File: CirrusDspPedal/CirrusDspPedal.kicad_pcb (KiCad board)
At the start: 2 copper layers, 112.5 x 86.4 mm, 92 parts, among them J1 MonoJack2Switch, J2 MonoJack2Switch, J3 Conn_02x05_Odd_Even, J4 Barrel_Jack_Switch, J5 MonoJack2Switch, J6 Micro_SD_Card, J7 Conn_01x01, K1 HFD4/3_S, Q1 DMG2302U, SW1 P26L-1D-RND MTL, SW2 P26L-1D-RND MTL, SW3 SW_SPST, SW4 SW_SPST, U1 CS5343, U2 74AHC1G126, U3 CS4344, U4 SE8250X2_SOT23, U5 MCP1703A-1202_SOT223, U6 MCP601-xOT, U7 STM32F405RGTx

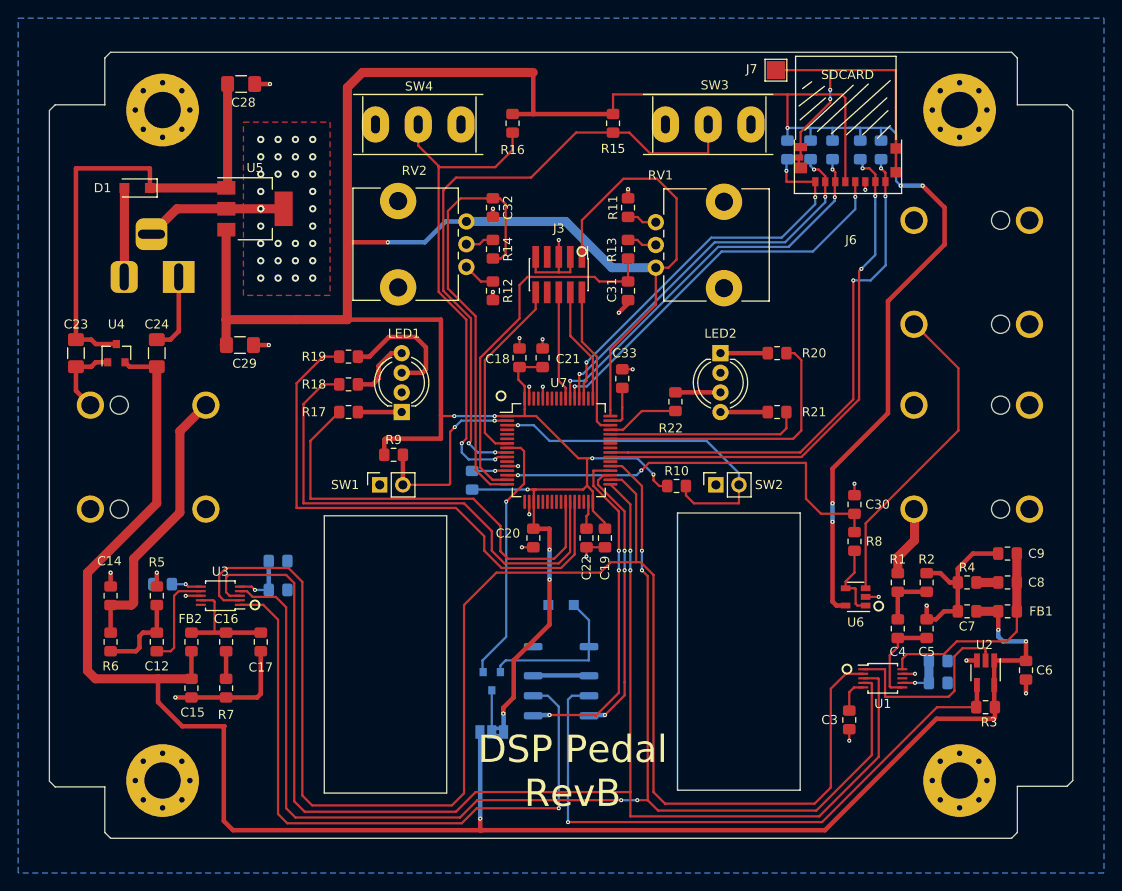
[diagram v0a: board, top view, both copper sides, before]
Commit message: Updated RevB
- Replaced analog pots with Rotary Encoders
- Added I2C connector (for OLED screen)
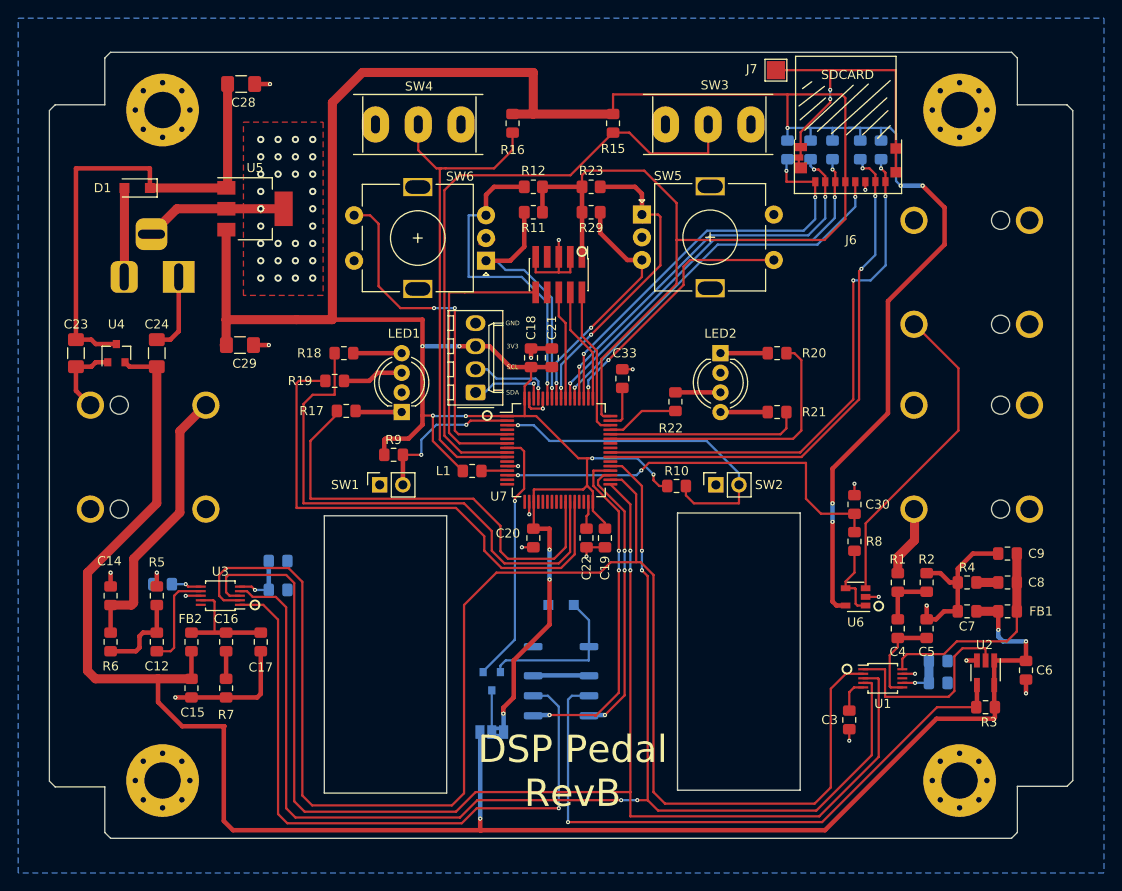
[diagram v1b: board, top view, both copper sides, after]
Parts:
- removed C31, C32: 100nF, Capacitor_SMD:C_0805_2012Metric_Pad1.15x1.40mm_HandSolder
- removed R13, R14: 50R, Resistor_SMD:R_0805_2012Metric_Pad1.15x1.40mm_HandSolder
- removed RV1, RV2: RK09L1140A65, Potentiometer_THT:Potentiometer_Alps_RK09L_Single_Vertical
- added J8: Conn_01x04, Connector_Molex:Molex_KK-254_AE-6410-04A_1x04_P2.54mm_Vertical, F.Cu at (139.2, 91.9)
- added R23: 10K, Resistor_SMD:R_0805_2012Metric_Pad1.20x1.40mm_HandSolder, F.Cu at (151.9, 69.3)
- added R29: 10K, Resistor_SMD:R_0805_2012Metric_Pad1.20x1.40mm_HandSolder, F.Cu at (151.9, 72.1)
- added SW5: Rotary_Encoder_Switch, Rotary_Encoder:RotaryEncoder_Alps_EC11E-Switch_Vertical_H20mm, F.Cu at (157.5, 72.4)
- added SW6: Rotary_Encoder_Switch, Rotary_Encoder:RotaryEncoder_Alps_EC11E-Switch_Vertical_H20mm, F.Cu at (140.3, 77.5)
- L1: moved to F.Cu
- R11, R12: value 100R -> 10K; footprint Resistor_SMD:R_0805_2012Metric_Pad1.15x1.40mm_HandSolder -> Resistor_SMD:R_0805_2012Metric_Pad1.20x1.40mm_HandSolder
- moved R12 12.3 mm to (145.5, 69.3), turned to 180 degrees
- moved R11 10.4 mm to (145.5, 72.1), turned to 180 degrees
- moved R18 3.47 mm to (124.7, 87.6)
- moved R19 3.07 mm to (123.7, 90.7)
- moved C18 1.27 mm to (145.3, 88.1)
- moved C21 1.02 mm to (147.6, 88.1)
- moved L1 1.02 mm to (138.8, 100.6), turned to 0 degrees
- moved R17 0.28 mm to (125.0, 94.0)
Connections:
- R11 pad 1: Net-(R11-Pad1) -> +3V3
- R11 pad 2: GND -> /ExtInput/Encoder2_ENC_A
- R12 pad 1: Net-(R12-Pad1) -> +3V3
- R12 pad 2: GND -> /ExtInput/Encoder2_ENC_B
- U7 pad 15: /ExtInput/UserPotA_IN -> Net-(U7-Pad15)
- U7 pad 16: /ExtInput/UserPotB_IN -> Net-(U7-Pad16)
- U7 pad 5: Net-(U7-Pad5) -> /ExtInput/Encoder2_ENC_SW
- U7 pad 50: Net-(U7-Pad50) -> /ExtInput/Encoder1_ENC_SW
- U7 pad 56: Net-(U7-Pad56) -> /ExtInput/Encoder1_ENC_A
- U7 pad 57: Net-(U7-Pad57) -> /ExtInput/Encoder1_ENC_B
- U7 pad 58: Net-(U7-Pad58) -> /ExtInput/Encoder2_ENC_A
- U7 pad 59: Net-(U7-Pad59) -> /ExtInput/Encoder2_ENC_B
- U7 pad 61: Net-(U7-Pad61) -> /SignalProcessing/OLED_SCL
- U7 pad 62: Net-(U7-Pad62) -> /SignalProcessing/OLED_SDA
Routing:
- net /ExtInput/UserPotB_IN: track 48.8 -> 0.00 mm
- net /ExtInput/UserPotA_IN: track 40.4 -> 0.00 mm
- net /ExtInput/Encoder2_ENC_SW: track 0.00 -> 38.7 mm, vias 0 -> 2
- net /ExtInput/Encoder2_ENC_B: track 0.00 -> 35.9 mm, vias 0 -> 1
- net /ExtInput/Encoder1_ENC_A: track 0.00 -> 34.7 mm, vias 0 -> 2
- net /ExtInput/Encoder1_ENC_SW: track 0.00 -> 29.1 mm, vias 0 -> 2
- net /ExtInput/Encoder2_ENC_A: track 0.00 -> 28.7 mm, vias 0 -> 1
- net /ExtInput/Encoder1_ENC_B: track 0.00 -> 27.2 mm, vias 0 -> 2
- net /SignalProcessing/NRST: track 20.7 -> 31.8 mm
- net /SignalProcessing/OLED_SCL: track 0.00 -> 9.34 mm, vias 0 -> 1
- net /SignalProcessing/OLED_SDA: track 0.00 -> 8.44 mm, vias 0 -> 1
- net Net-(LED1-Pad3): track 14.1 -> 6.71 mm
- net +3V3: track 419.2 -> 426.0 mm
- net /ExtInput/FootSwitchA_IN: track 21.0 -> 17.3 mm
- net /SignalProcessing/LEDA_G: track 55.1 -> 58.8 mm
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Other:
- board text added: "GND"
- board text added: "SCL"
- board text added: "SDA"

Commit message: updated revB
- Added higher out current LDO (LD1117) for 5V rail
- Added jumper on OLED connector to select 3V3/5V
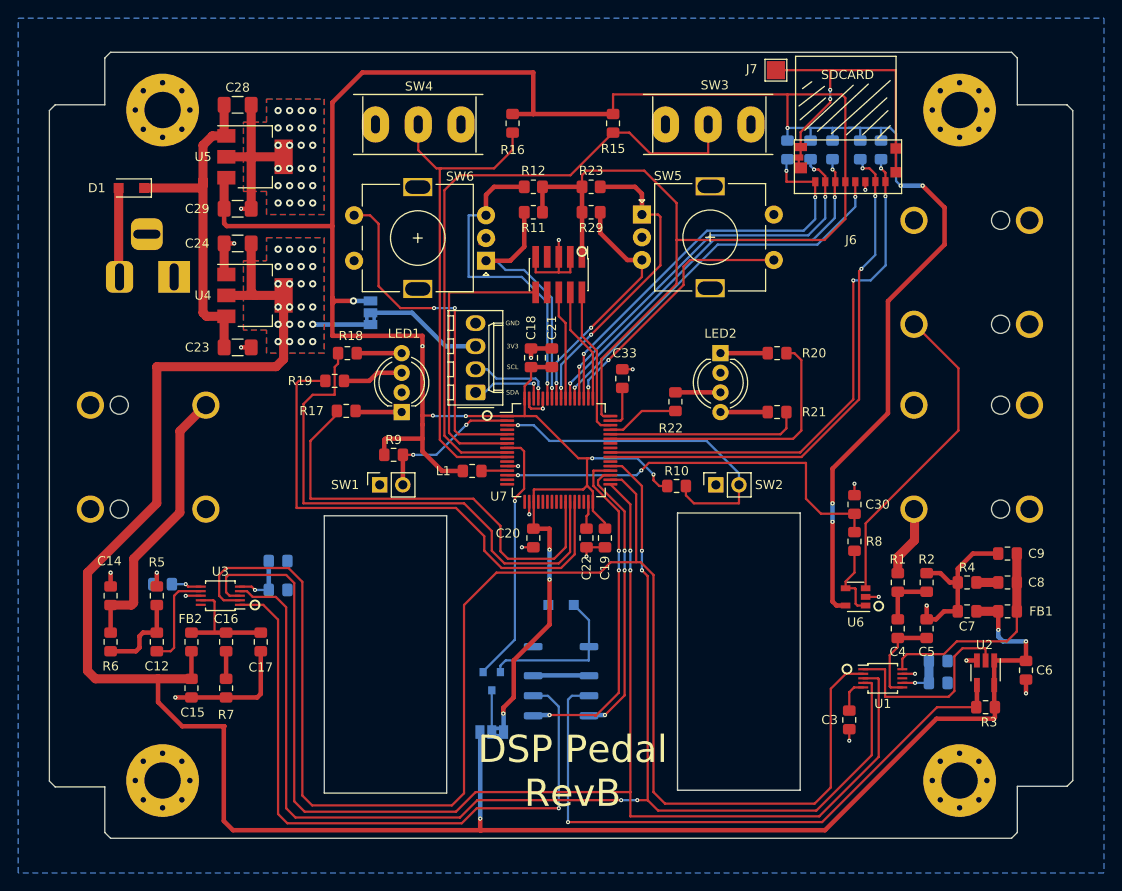
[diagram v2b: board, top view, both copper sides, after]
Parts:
- added JP1: Jumper_3_Bridged12, Jumper:SolderJumper-3_P1.3mm_Bridged2Bar12_Pad1.0x1.5mm, B.Cu at (127.6, 83.2)
- C23: value 1uF -> 100nF 25V
- C24: value 1uF -> 10uF
- C28: value 1uF -> 1uF 25V
- U4: value SE8250X2_SOT23 -> LD1117S50TR_SOT223; footprint Package_TO_SOT_SMD:SOT-23 -> Package_TO_SOT_SMD:SOT-223-3_TabPin2
- moved C23 17.8 mm to (113.0, 87.0), turned to 0 degrees
- moved U4 16.5 mm to (114.9, 81.3), turned to 0 degrees
- moved C29 15.0 mm to (113.0, 71.8)
- moved C24 15.0 mm to (113.0, 75.6), turned to 180 degrees
- moved U5 5.71 mm to (114.9, 66.0)
- moved C28 2.32 mm to (113.0, 60.3)
- moved D1 0.63 mm to (101.3, 69.5)
- moved J4 0.51 mm to (106.0, 79.2)
- moved R18 0.38 mm to (125.1, 87.6)
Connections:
- J8 pad 3: +3V3 -> Net-(J8-Pad3)
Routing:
- net +5V: track 197.7 -> 233.9 mm, vias 3 -> 27
- net +3V3: track 426.0 -> 406.8 mm
- net Net-(C23-Pad1): track 53.7 -> 38.4 mm
- net Net-(J8-Pad3): track 0.00 -> 13.1 mm
- net GND: track 112.0 -> 100.1 mm, vias 52 -> 47
- net /ExtInput/FootSwitchA_IN: track 17.3 -> 16.3 mm
- added copper zone on B.Cu, net +5V
- added copper zone on F.Cu, net +5V
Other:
- rule pad_to_mask_clearance: 0.05 -> 0
- board text added: "<- OLED"

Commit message: updated revb
- Added input amp with charge pump and protection diodes
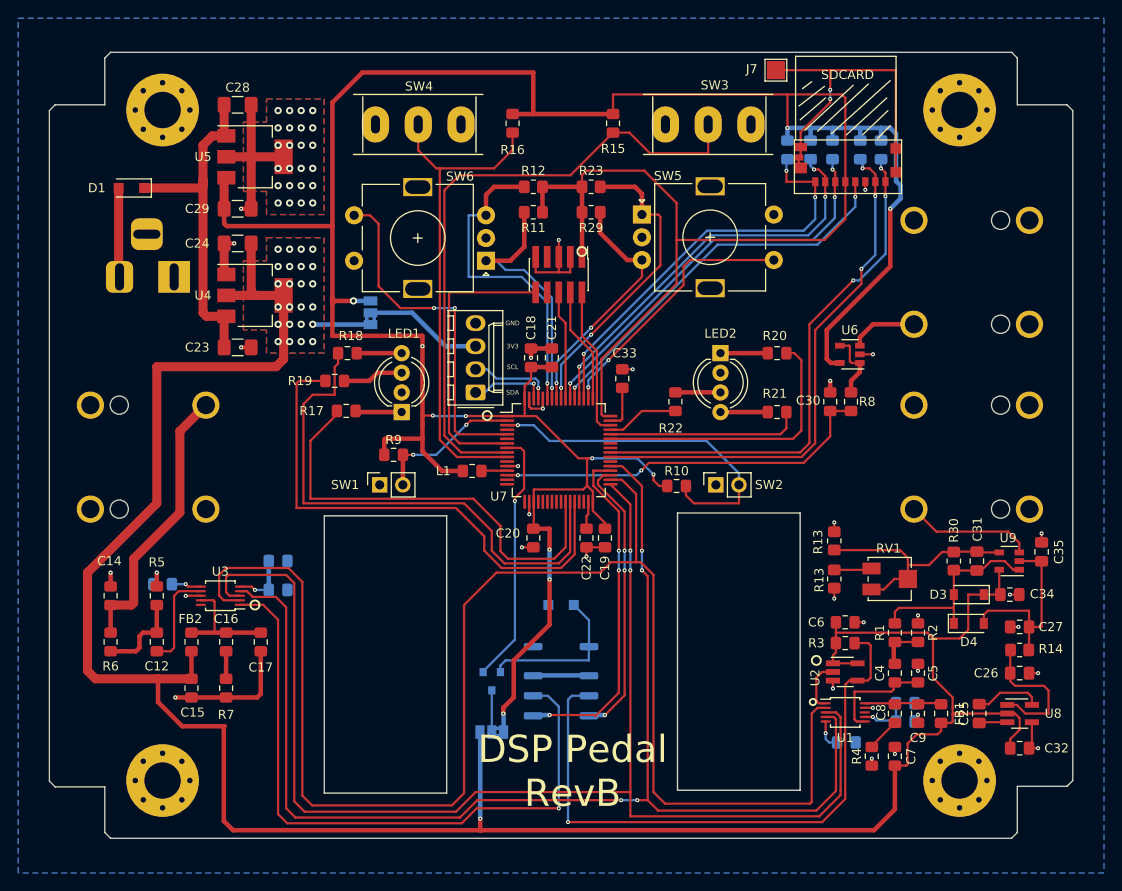
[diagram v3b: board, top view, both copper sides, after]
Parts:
- added C25: 1uF, Capacitor_SMD:C_0805_2012Metric_Pad1.18x1.45mm_HandSolder, F.Cu at (194.6, 127.3)
- added C26: 1uF, Capacitor_SMD:C_0805_2012Metric_Pad1.18x1.45mm_HandSolder, F.Cu at (199.0, 122.8)
- added C27: 100nF, Capacitor_SMD:C_0805_2012Metric_Pad1.18x1.45mm_HandSolder, F.Cu at (199.0, 117.7)
- added C31: 270pF, Capacitor_SMD:C_0805_2012Metric_Pad1.18x1.45mm_HandSolder, F.Cu at (194.3, 110.5)
- added C32: 1uF, Capacitor_SMD:C_0805_2012Metric_Pad1.18x1.45mm_HandSolder, F.Cu at (199.0, 131.1)
- added C34: 100nF, Capacitor_SMD:C_0805_2012Metric_Pad1.18x1.45mm_HandSolder, F.Cu at (197.9, 114.2)
- added C35: 100nF, Capacitor_SMD:C_0805_2012Metric_Pad1.18x1.45mm_HandSolder, F.Cu at (201.4, 109.5)
- added D3: 1N5817, Diode_SMD:D_SOD-123, F.Cu at (193.4, 114.2)
- added D4: 1N5817, Diode_SMD:D_SOD-123, F.Cu at (193.4, 117.3)
- added R13: 4K7, Resistor_SMD:R_0805_2012Metric_Pad1.20x1.40mm_HandSolder, F.Cu at (178.6, 112.5)
- added R13: 10K, Resistor_SMD:R_0805_2012Metric_Pad1.20x1.40mm_HandSolder, F.Cu at (178.6, 108.3)
- added R14: 47R, Resistor_SMD:R_0805_2012Metric_Pad1.20x1.40mm_HandSolder, F.Cu at (199.0, 120.3)
- added R30: 100K, Resistor_SMD:R_0805_2012Metric_Pad1.20x1.40mm_HandSolder, F.Cu at (191.8, 110.5)
- added RV1: 500K, Potentiometer_SMD:Potentiometer_Bourns_3314J_Vertical, F.Cu at (184.7, 112.5)
- added U8: TPS60400, Package_TO_SOT_SMD:SOT-23-5_HandSoldering, F.Cu at (199.0, 127.3)
- added U9: OPA209AIDBV, Package_TO_SOT_SMD:SOT-23-5, F.Cu at (197.9, 110.5)
- C3: moved to B.Cu
- moved U6 26.7 mm to (180.3, 87.8)
- moved R4 21.8 mm to (182.8, 132.0), turned to 270 degrees
- moved C6 20.6 mm to (179.8, 117.2), turned to 0 degrees
- moved C9 20.2 mm to (187.8, 127.3), turned to 270 degrees
- moved C8 19.0 mm to (185.3, 127.3), turned to 270 degrees
- moved C7 17.8 mm to (185.3, 132.0), turned to 90 degrees
- moved R3 17.0 mm to (179.8, 119.5), turned to 180 degrees
- moved U2 15.4 mm to (179.8, 122.7), turned to 0 degrees
- moved R8 15.4 mm to (180.5, 93.0), turned to 90 degrees
- moved FB1 13.4 mm to (190.4, 127.3), turned to 270 degrees
- moved C30 11.6 mm to (178.2, 93.0)
- moved C1 5.88 mm to (186.4, 126.1)
- moved R2 5.61 mm to (187.8, 118.4)
- moved C2 5.59 mm to (186.4, 128.1)
- moved U1 5.57 mm to (179.8, 127.1)
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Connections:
- R1 pad 2: Net-(J1-Pad1) -> Net-(C31-Pad1)
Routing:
- net +5V: track 233.9 -> 267.5 mm, vias 27 -> 25
- net +3V3: track 406.8 -> 375.0 mm, vias 14 -> 11
- net Net-(J5-Pad1): track 35.3 -> 7.52 mm
- net Net-(C31-Pad2): track 0.00 -> 26.1 mm
- net Net-(C31-Pad1): track 0.00 -> 22.2 mm
- net -5V: track 0.00 -> 21.0 mm
- net /InputSignal/SDOUT: track 22.3 -> 5.76 mm
- net Net-(C26-Pad1): track 0.00 -> 15.5 mm
- net /InputSignal/VA: track 23.5 -> 8.85 mm
- net Net-(C25-Pad2): track 0.00 -> 7.38 mm
- net GND: track 100.1 -> 93.0 mm, vias 47 -> 57
- net /InputSignal/ADIN_SCLK: track 171.9 -> 165.4 mm
- net Net-(J1-Pad1): track 7.83 -> 14.3 mm
- net /InputSignal/ADIN_LRCK: track 151.4 -> 145.7 mm
- net /InputSignal/ADIN_MCLK: track 144.5 -> 139.4 mm
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
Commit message: updated revb
- Moved THT components to improve UX layout
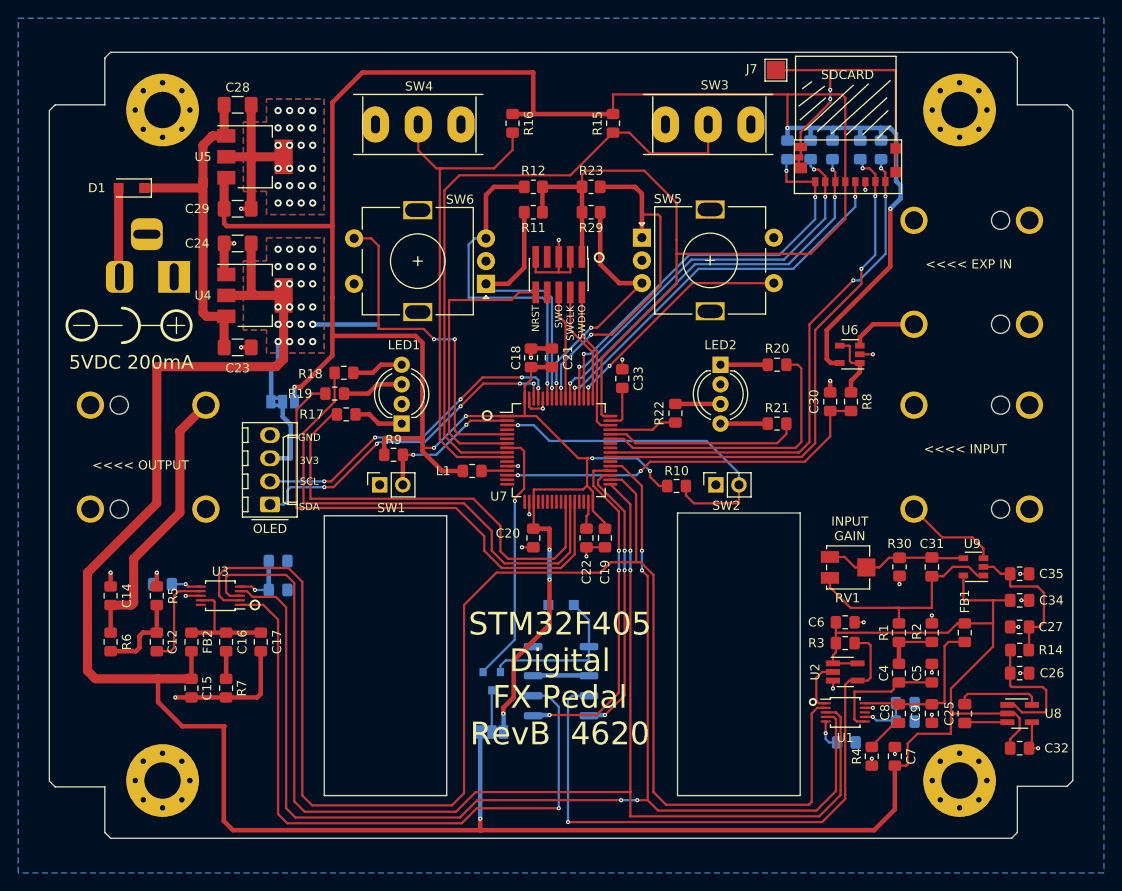
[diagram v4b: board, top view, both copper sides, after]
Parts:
- removed D3, D4: 1N5817, Diode_SMD:D_SOD-123
- removed R13: 4K7, Resistor_SMD:R_0805_2012Metric_Pad1.20x1.40mm_HandSolder
- removed R13: 10K, Resistor_SMD:R_0805_2012Metric_Pad1.20x1.40mm_HandSolder
- RV1: value 500K -> 100K
- moved J8 25.7 mm to (116.6, 104.3)
- moved JP1 13.7 mm to (118.0, 93.0), turned to 0 degrees
- moved FB1 9.26 mm to (193.0, 118.4), turned to 90 degrees
- moved R30 6.00 mm to (185.8, 111.1), turned to 270 degrees
- moved C31 4.99 mm to (189.4, 111.1)
- moved RV1 4.75 mm to (180.1, 111.2)
- moved U9 3.99 mm to (193.9, 111.1)
- moved C35 3.41 mm to (199.0, 111.9), turned to 0 degrees
- moved SW5 2.54 mm to (157.5, 74.9)
- moved SW6 2.54 mm to (140.3, 80.0)
- moved R18 2.19 mm to (124.7, 89.8)
- moved C25 1.59 mm to (193.0, 127.3)
- moved C5 1.52 mm to (189.4, 122.8)
- moved C9 1.52 mm to (189.4, 127.3)
- moved R2 1.52 mm to (189.4, 118.4)
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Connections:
- R30 pad 1: Net-(C31-Pad1) -> Net-(C31-Pad2)
- R30 pad 2: Net-(C31-Pad2) -> GND
- RV1 pad 1: Net-(R13-Pad1) -> Net-(C31-Pad2)
- RV1 pad 3: Net-(C31-Pad2) -> Net-(C31-Pad1)
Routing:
- net /SignalProcessing/OLED_SDA: track 8.44 -> 36.8 mm, vias 1 -> 5
- net /SignalProcessing/OLED_SCL: track 9.34 -> 36.4 mm, vias 1 -> 5
- net +5V: track 267.5 -> 281.1 mm
- net Net-(C31-Pad2): track 26.1 -> 16.2 mm
- net /InputSignal/VA: track 8.85 -> 17.9 mm
- net +3V3: track 375.0 -> 381.0 mm, vias 11 -> 10
- net -5V: track 21.0 -> 16.3 mm
- net Net-(J8-Pad3): track 13.1 -> 8.88 mm
- net Net-(R13-Pad1): track 4.16 -> 0.00 mm
- net /SignalProcessing/LEDA_G: track 59.0 -> 55.1 mm
- net /ExtInput/Encoder1_ENC_A: track 34.7 -> 38.5 mm
- net GND: track 93.0 -> 89.2 mm, vias 57 -> 56
- net Net-(J1-Pad1): track 14.3 -> 10.6 mm
- net Net-(C31-Pad1): track 22.2 -> 25.4 mm
- net /ExtInput/Encoder1_ENC_SW: track 29.1 -> 26.4 mm
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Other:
- outline, holes or cut-outs redrawn
- board text added: "5VDC 200mA"
- board text added: "<<<< EXP IN"
- board text added: "<<<< INPUT"
- board text added: "<<<< OUTPUT"
- board text added: "INPUT GAIN"
- board text added: "NRST"
- board text added: "OLED"
- board text added: "STM32F405 Digital FX Pedal RevB 4620"
- board text added: "SWCLK"
- board text added: "SWDIO"
- board text added: "SWO"
- board text removed: "DSP Pedal RevB"

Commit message: final revb layout
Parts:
- added D3: LED, LED_SMD:LED_0805_2012Metric_Pad1.15x1.40mm_HandSolder, F.Cu at (198.9, 119.3)
- added D4: LED, LED_SMD:LED_0805_2012Metric_Pad1.15x1.40mm_HandSolder, F.Cu at (120.3, 57.4)
- added D5: LED, LED_SMD:LED_0805_2012Metric_Pad1.15x1.40mm_HandSolder, F.Cu at (120.3, 91.7)
- added R13: 2K2, Resistor_SMD:R_0805_2012Metric_Pad1.20x1.40mm_HandSolder, F.Cu at (198.9, 121.9)
- added R31: 2K2, Resistor_SMD:R_0805_2012Metric_Pad1.20x1.40mm_HandSolder, F.Cu at (115.8, 57.4)
- added R32: 2K2, Resistor_SMD:R_0805_2012Metric_Pad1.20x1.40mm_HandSolder, F.Cu at (115.8, 91.7)
- SW5, SW6: value Rotary_Encoder_Switch -> PEC11R-4020K-S0024
- U9: value OPA209AIDBV -> OPA197IDBV
- moved C26 4.59 mm to (195.6, 125.9), turned to 270 degrees
- moved R14 3.56 mm to (198.9, 116.7)
- moved C27 3.56 mm to (198.9, 114.2)
- moved C34 3.18 mm to (198.9, 111.6)
- moved C35 2.79 mm to (198.9, 109.1)
- moved R19 2.16 mm to (125.9, 92.1)
- moved C32 1.73 mm to (199.7, 129.5)
- moved U8 1.62 mm to (199.7, 125.8)
- moved C25 1.46 mm to (193.0, 125.8)
- moved R18 1.14 mm to (125.9, 89.8)
- moved R17 0.89 mm to (125.9, 94.4)
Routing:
- net +5V: track 281.1 -> 290.1 mm
- net Net-(C26-Pad1): track 15.1 -> 21.3 mm
- net +3V3: track 381.0 -> 384.8 mm
- net GND: track 89.2 -> 92.5 mm, vias 56 -> 59
- net Net-(C25-Pad1): track 4.72 -> 7.93 mm
- net /SignalProcessing/LEDA_G: track 55.1 -> 58.1 mm
- net Net-(D3-Pad2): track 0.00 -> 2.61 mm
- net Net-(D5-Pad1): track 0.00 -> 2.42 mm
- net Net-(D4-Pad1): track 0.00 -> 2.42 mm
- net Net-(LED1-Pad3): track 6.76 -> 4.48 mm
- net Net-(LED1-Pad4): track 5.69 -> 4.42 mm
- net Net-(LED1-Pad1): track 5.49 -> 4.48 mm
- net Net-(C25-Pad2): track 9.33 -> 10.2 mm
- net /SignalProcessing/LEDA_B: track 55.3 -> 56.1 mm
- net -5V: track 16.3 -> 15.5 mm
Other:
- board text added: "9VDC 200mA"
- board text added: "OLED VDD SELECTION"
- board text added: "RELAY DRIVER VOLT SELECT"
- board text removed: "5VDC 200mA"
- board text removed: "<- OLED"
